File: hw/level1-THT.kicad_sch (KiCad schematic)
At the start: 6 parts, among them J2 USB_A, U1 LM555xN

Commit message: level 1
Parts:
- added Klobouek?: redhatLogo, Robotarna_KiCad_Library:RedhatLogo, symbol Robotarna_KiCad_Library:redhatLogo
- added Kolecko?: robotarnaLogo, Robotarna_KiCad_Library:RobotarnaLogo-6mm, symbol Robotarna_KiCad_Library:robotarnaLogo
- added R2: 1M, Resistor_THT:R_Axial_DIN0207_L6.3mm_D2.5mm_P15.24mm_Horizontal, symbol Device:R
- C1: renamed from C2; value 4.7u -> 1u; footprint Capacitor_THT:C_Disc_D6.0mm_W2.5mm_P5.00mm -> Capacitor_THT:C_Disc_D7.5mm_W2.5mm_P5.00mm
- R1: value 1k -> 470; footprint Resistor_THT:R_Axial_DIN0204_L3.6mm_D1.6mm_P5.08mm_Horizontal -> Resistor_THT:R_Axial_DIN0207_L6.3mm_D2.5mm_P15.24mm_Horizontal
- R3: value 330 -> 470; footprint Resistor_THT:R_Axial_DIN0204_L3.6mm_D1.6mm_P5.08mm_Horizontal -> Resistor_THT:R_Axial_DIN0207_L6.3mm_D2.5mm_P15.24mm_Horizontal
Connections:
- net GND: now also R3.2
- net VCC: now also R1.1
- net at C1.1, U1.2 (TR), U1.6 (THR): now also R2.1; no longer R1.1, R3.2
- net at D1.2 (A), U1.3 (Q): now also R2.2; no longer R3.1
- net at D1.1 (K), R1.2: now also R3.1
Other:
- moved on the sheet: D1, R1

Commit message: Level 2 and 3
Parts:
- gave numbers to parts that had none: 2
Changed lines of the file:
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@@
   (symbol (lib_id "Device:R") (at 220.345 88.9 0) (unit 1)
     (in_bom yes) (on_board yes)
-    (property "Reference" "R1" (id 0) (at 215.0872 88.9 90))
-    (property "Value" "470" (id 1) (at 217.3986 88.9 90))
+    (property "Reference" "R1" (id 0) (at 215.9 87.8586 0))
+    (property "Value" "470" (id 1) (at 215.9 90.17 0))
     (property "Footprint" "Resistor_THT:R_Axial_DIN0207_L6.3mm_D2.5mm_P15.24mm_Horizontal" (id 2) (at 218.567 88.9 90)
       (effects (font (size 1.27 1.27)) hide)
@@
     (pin "2")
   )
-  (symbol (lib_id "Robotarna_KiCad_Library:robotarnaLogo") (at 248.92 88.9 0) (unit 1)
+  (symbol (lib_id "Robotarna_KiCad_Library:robotarnaLogo") (at 240.665 99.06 0) (unit 1)
     (in_bom yes) (on_board yes) (fields_autoplaced)
-    (property "Reference" "Kolecko?" (id 0) (at 250.19 87.6299 0)
+    (property "Reference" "Kolecko1" (id 0) (at 241.935 97.7899 0)
       (effects (font (size 1.27 1.27)) (justify left))
     )
-    (property "Value" "robotarnaLogo" (id 1) (at 250.19 90.1699 0)
+    (property "Value" "robotarnaLogo" (id 1) (at 241.935 100.3299 0)
       (effects (font (size 1.27 1.27)) (justify left))
     )
-    (property "Footprint" "Robotarna_KiCad_Library:RobotarnaLogo-6mm" (id 2) (at 248.92 86.36 0)
+    (property "Footprint" "Robotarna_KiCad_Library:RobotarnaLogo-6mm" (id 2) (at 240.665 96.52 0)
       (effects (font (size 1.27 1.27)) hide)
     )
-    (property "Datasheet" "" (id 3) (at 248.92 88.9 0)
+    (property "Datasheet" "" (id 3) (at 240.665 99.06 0)
       (effects (font (size 1.27 1.27)) hide)
     )
@@
   (symbol (lib_id "Device:R") (at 220.345 105.41 0) (unit 1)
     (in_bom yes) (on_board yes)
-    (property "Reference" "R3" (id 0) (at 215.0872 105.41 90))
-    (property "Value" "470" (id 1) (at 217.3986 105.41 90))
+    (property "Reference" "R3" (id 0) (at 215.9 106.4514 0))
+    (property "Value" "470" (id 1) (at 215.9 104.14 0))
     (property "Footprint" "Resistor_THT:R_Axial_DIN0207_L6.3mm_D2.5mm_P15.24mm_Horizontal" (id 2) (at 218.567 105.41 90)
       (effects (font (size 1.27 1.27)) hide)
@@
     (pin "2")
   )
-  (symbol (lib_id "Robotarna_KiCad_Library:redhatLogo") (at 249.555 81.28 0) (unit 1)
+  (symbol (lib_id "Robotarna_KiCad_Library:redhatLogo") (at 241.3 91.44 0) (unit 1)
     (in_bom yes) (on_board yes) (fields_autoplaced)
-    (property "Reference" "Klobouek?" (id 0) (at 250.19 80.0099 0)
+    (property "Reference" "Klobouek1" (id 0) (at 241.935 90.1699 0)
       (effects (font (size 1.27 1.27)) (justify left))
     )
-    (property "Value" "redhatLogo" (id 1) (at 250.19 82.5499 0)
+    (property "Value" "redhatLogo" (id 1) (at 241.935 92.7099 0)
       (effects (font (size 1.27 1.27)) (justify left))
     )
-    (property "Footprint" "Robotarna_KiCad_Library:RedhatLogo" (id 2) (at 249.555 78.74 0)
+    (property "Footprint" "Robotarna_KiCad_Library:RedhatLogo" (id 2) (at 241.3 88.9 0)
       (effects (font (size 1.27 1.27)) hide)
     )
-    (property "Datasheet" "" (id 3) (at 249.555 81.28 0)
+    (property "Datasheet" "" (id 3) (at 241.3 91.44 0)
       (effects (font (size 1.27 1.27)) hide)
     )

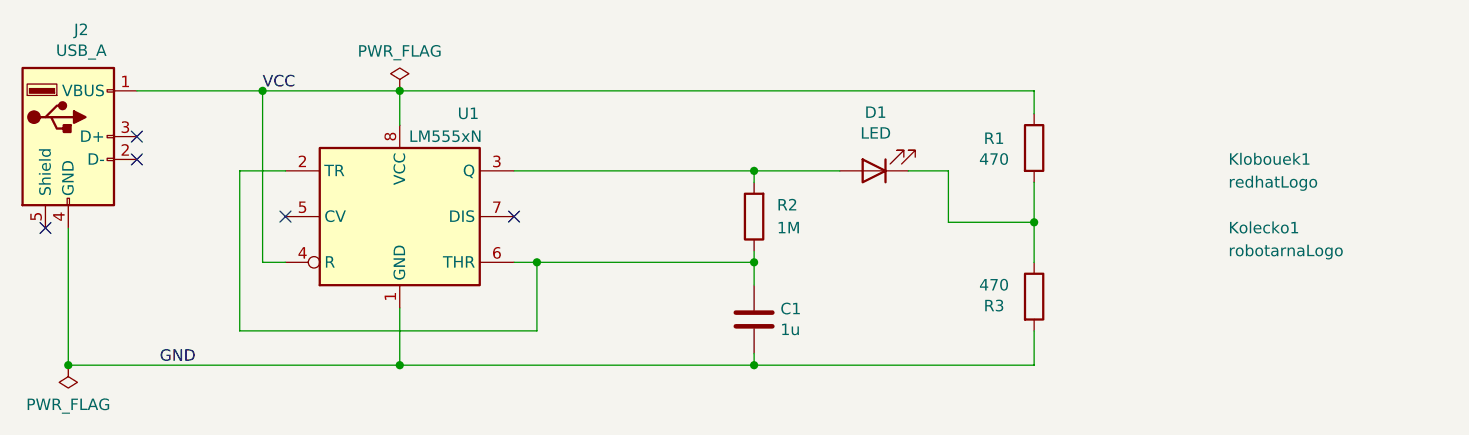
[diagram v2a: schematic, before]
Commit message: Resistor labels
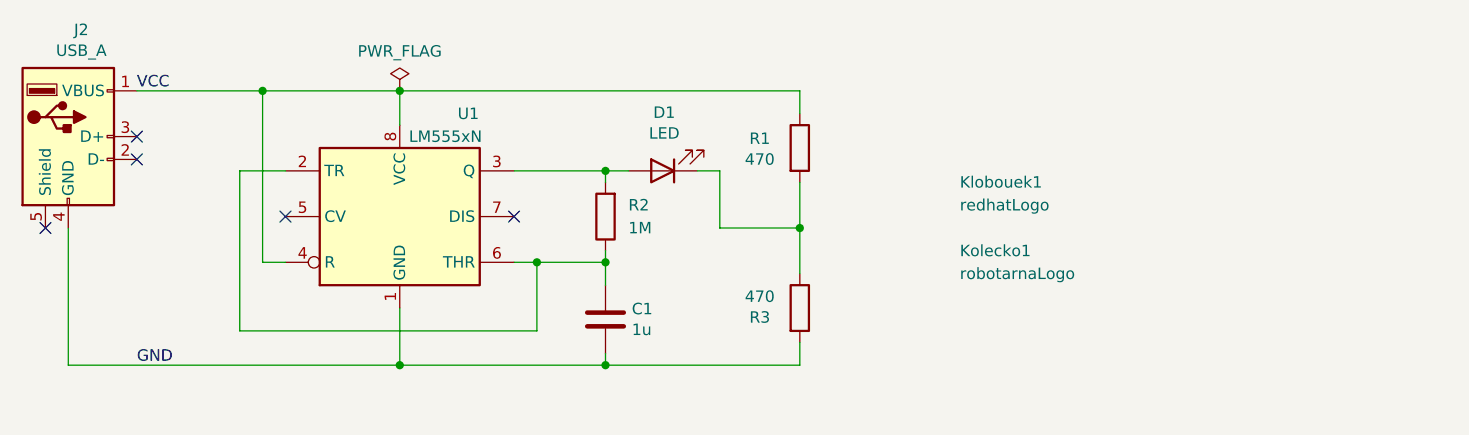
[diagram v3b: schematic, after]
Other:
- moved on the sheet: C1, D1, R1, R2, R3
